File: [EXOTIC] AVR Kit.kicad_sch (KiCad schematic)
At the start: 24 parts, among them J2 AVR-ISP-10, J3 USB_B, J4 Port A, J5 Port B, J6 Port C + D7, J7 Port D, SW1 SW_Push, U1 ATmega32A-P, U6 CH340C, Y1 16 MHz

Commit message: Pre Rev. 4
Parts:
- added F2: Polyfuse_Small, Capacitor_THT:C_Disc_D10.5mm_W5.0mm_P5.00mm, symbol Device:Polyfuse_Small
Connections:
- net +5V: now also F2.1; no longer R1.1, U1.10 (VCC)
- new net +5V_{PPTC}: F2.2, R1.1, U1.10 (VCC)
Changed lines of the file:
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@@
+    (stroke (width 0) (type default))
+  )
+  (wire (pts (xy 110.49 31.75) (xy 110.49 34.29))
     (stroke (width 0) (type default))
   )
@@
     (stroke (width 0) (type default))
   )
+  (wire (pts (xy 110.49 41.91) (xy 110.49 39.37))
+    (stroke (width 0) (type default))
+  )
   (wire (pts (xy 146.05 127) (xy 151.13 127))
     (stroke (width 0) (type default))
@@
     (stroke (width 0) (type default))
   )
-  (wire (pts (xy 90.17 30.48) (xy 92.71 30.48))
-    (stroke (width 0) (type default))
-  )
   (wire (pts (xy 60.96 26.67) (xy 60.96 29.21))
     (stroke (width 0) (type default))
@@
     (stroke (width 0) (type default))
   )
+  (wire (pts (xy 90.17 30.48) (xy 95.25 30.48))
+    (stroke (width 0) (type default))
+  )
   (wire (pts (xy 91.44 121.92) (xy 93.98 121.92))
     (stroke (width 0) (type default))
@@
   )
   (wire (pts (xy 91.44 132.08) (xy 93.98 132.08))
-    (stroke (width 0) (type default))
-  )
-  (wire (pts (xy 92.71 27.94) (xy 92.71 30.48))
     (stroke (width 0) (type default))
   )
@@
   (label "PD5" (at 93.98 132.08 0) (fields_autoplaced)
     (effects (font (size 1.27 1.27)) (justify left bottom))
+  )
+  (global_label "+5V_{PPTC}" (shape input) (at 60.96 26.67 90) (fields_autoplaced)
+    (effects (font (size 1.27 1.27)) (justify left))
+    (property "Intersheetrefs" "${INTERSHEET_REFS}" (at 60.96 15.9414 90)
+      (effects (font (size 1.27 1.27)) (justify left) hide)
+    )
   )
   (global_label "+5V_{NetTie}" (shape input) (at 171.45 34.29 90) (fields_autoplaced)
@@
     )
   )
-  (global_label "+5V_{NetTie}" (shape input) (at 92.71 27.94 90) (fields_autoplaced)
+  (global_label "+5V_{PPTC}" (shape input) (at 97.79 19.05 0) (fields_autoplaced)
     (effects (font (size 1.27 1.27)) (justify left))
-    (property "Intersheetrefs" "${INTERSHEET_REFS}" (at 92.71 16.3888 90)
+    (property "Intersheetrefs" "${INTERSHEET_REFS}" (at 108.5186 19.05 0)
       (effects (font (size 1.27 1.27)) (justify left) hide)
     )
   )
-  (symbol (lib_id "power:+5V") (at 76.2 40.64 0) (unit 1)
-    (in_bom yes) (on_board yes) (dnp no) (fields_autoplaced)
-    (property "Reference" "#PWR06" (at 76.2 44.45 0)
-      (effects (font (size 1.27 1.27)) hide)
-    )
-    (property "Value" "+5V" (at 76.2 36.83 0)
-      (effects (font (size 1.27 1.27)))
-    )
-    (property "Footprint" "" (at 76.2 40.64 0)
-      (effects (font (size 1.27 1.27)) hide)
-    )
-    (property "Datasheet" "" (at 76.2 40.64 0)
+  (global_label "+5V_{PPTC}" (shape output) (at 110.49 41.91 270) (fields_autoplaced)
+    (effects (font (size 1.27 1.27)) (justify right))
+    (property "Intersheetrefs" "${INTERSHEET_REFS}" (at 110.49 52.6386 90)
+      (effects (font (size 1.27 1.27)) (justify right) hide)
+    )
+  )
+  (global_label "+5V_{PPTC}" (shape input) (at 76.2 40.64 90) (fields_autoplaced)
+    (effects (font (size 1.27 1.27)) (justify left))
+    (property "Intersheetrefs" "${INTERSHEET_REFS}" (at 76.2 29.9114 90)
+      (effects (font (size 1.27 1.27)) (justify left) hide)
+    )
+  )
+  (global_label "+5V_{NetTie}" (shape input) (at 95.25 30.48 0) (fields_autoplaced)
+    (effects (font (size 1.27 1.27)) (justify left))
+    (property "Intersheetrefs" "${INTERSHEET_REFS}" (at 106.8012 30.48 0)
+      (effects (font (size 1.27 1.27)) (justify left) hide)
+    )
+  )
+  (symbol (lib_id "power:+5V") (at 110.49 31.75 0) (unit 1)
+    (in_bom yes) (on_board yes) (dnp no)
+    (property "Reference" "#PWR06" (at 110.49 35.56 0)
+      (effects (font (size 1.27 1.27)) hide)
+    )
+    (property "Value" "+5V" (at 110.49 27.94 0)
+      (effects (font (size 1.27 1.27)))
+    )
+    (property "Footprint" "" (at 110.49 31.75 0)
+      (effects (font (size 1.27 1.27)) hide)
+    )
+    (property "Datasheet" "" (at 110.49 31.75 0)
       (effects (font (size 1.27 1.27)) hide)
     )
@@
     )
   )
-  (symbol (lib_id "power:+5V") (at 60.96 26.67 0) (unit 1)
-    (in_bom yes) (on_board yes) (dnp no) (fields_autoplaced)
-    (property "Reference" "#PWR05" (at 60.96 30.48 0)
-      (effects (font (size 1.27 1.27)) hide)
-    )
-    (property "Value" "+5V" (at 60.96 22.86 0)
-      (effects (font (size 1.27 1.27)))
-    )
-    (property "Footprint" "" (at 60.96 26.67 0)
-      (effects (font (size 1.27 1.27)) hide)
-    )
-    (property "Datasheet" "" (at 60.96 26.67 0)
-      (effects (font (size 1.27 1.27)) hide)
-    )
-    (pin "1")
-    (instances
-      (project "[EXOTIC] AVR Kit"
-        (path "/bd689b4b-40d7-46ba-91b6-965ce30f8212"
-          (reference "#PWR05") (unit 1)
-        )
-      )
-      (project "ATMEGA32A Development Board"
-        (path "/e232854a-3fe0-4443-9abe-081b69d86c79"
-          (reference "#PWR08") (unit 1)
-        )
-      )
-    )
-  )
   (symbol (lib_id "Connector:Conn_01x08_Socket") (at 181.61 119.38 0) (unit 1)
     (in_bom yes) (on_board yes) (dnp no) (fields_autoplaced)
@@
         )
       )
+    )
+  )
+  (symbol (lib_id "Device:Polyfuse_Small") (at 110.49 36.83 0) (unit 1)
+    (in_bom yes) (on_board yes) (dnp no) (fields_autoplaced)
+    (property "Reference" "F2" (at 113.03 35.56 0)
+      (effects (font (size 1.27 1.27)) (justify left))
+    )
+    (property "Value" "Polyfuse_Small" (at 113.03 38.1 0)
+      (effects (font (size 1.27 1.27)) (justify left))
+    )
+    (property "Footprint" "Capacitor_THT:C_Disc_D10.5mm_W5.0mm_P5.00mm" (at 111.76 41.91 0)
+      (effects (font (size 1.27 1.27)) (justify left) hide)
+    )
+    (property "Datasheet" "~" (at 110.49 36.83 0)
+      (effects (font (size 1.27 1.27)) hide)
+    )
+    (pin "1")
+    (pin "2")
+    (instances
+      (project "[EXOTIC] AVR Kit"
+        (path "/bd689b4b-40d7-46ba-91b6-965ce30f8212"
+          (reference "F2") (unit 1)
+        )
+      )

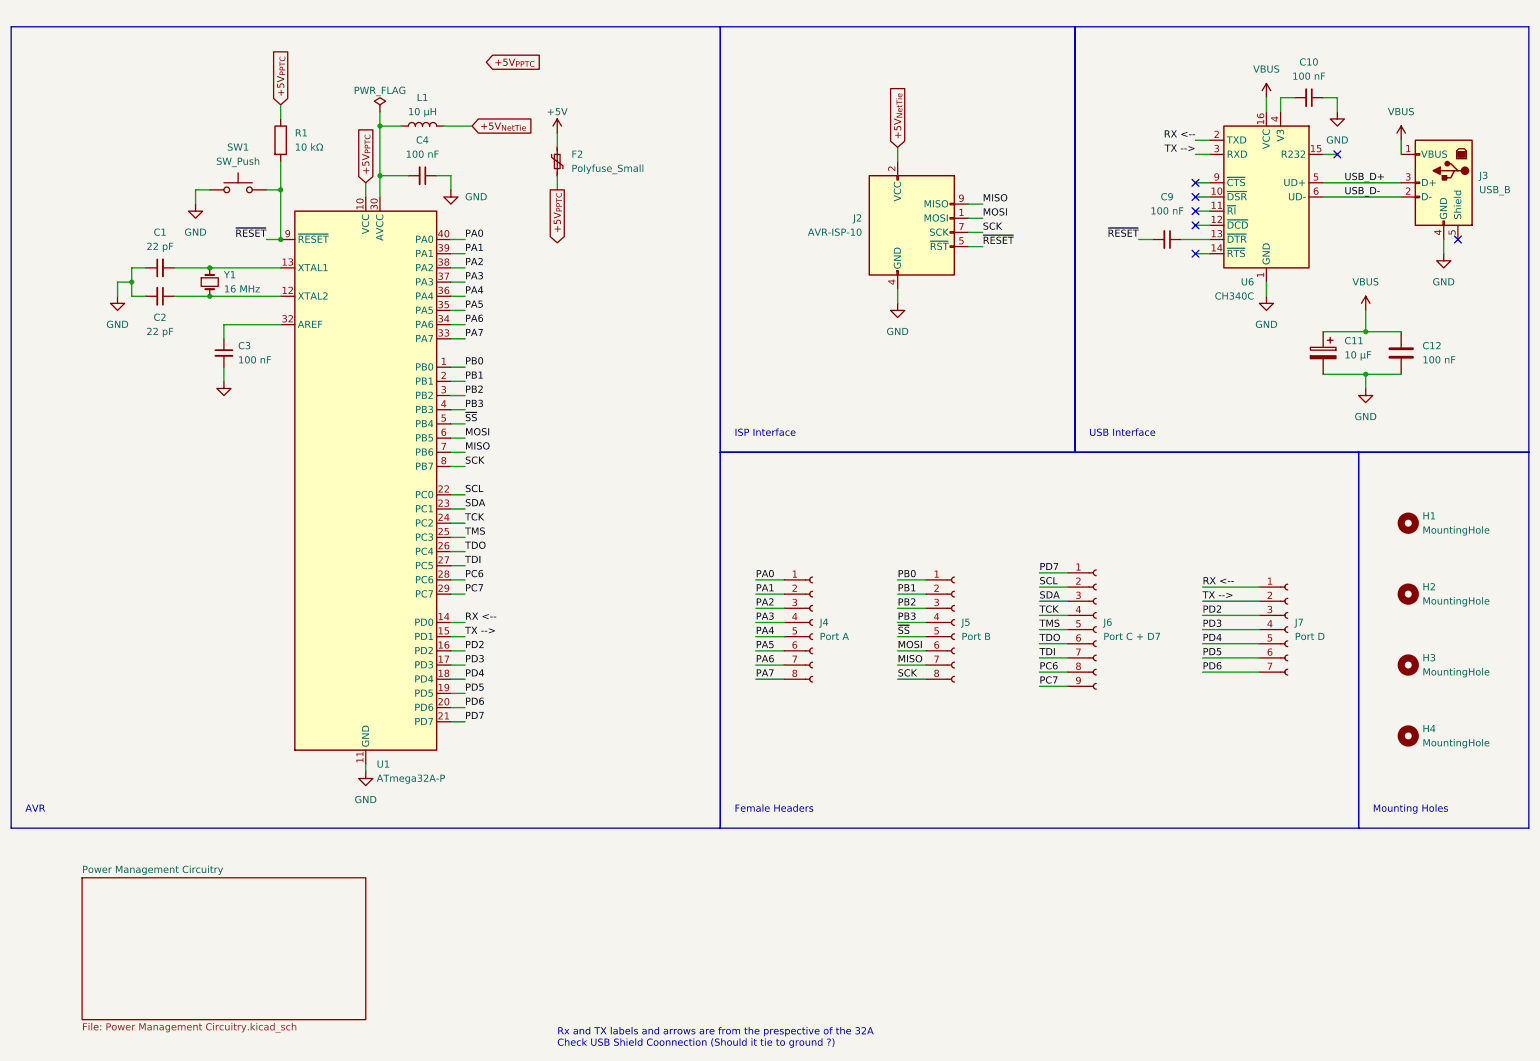
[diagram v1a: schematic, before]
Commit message: Migrated from KiCAD 7.0 to 8.0
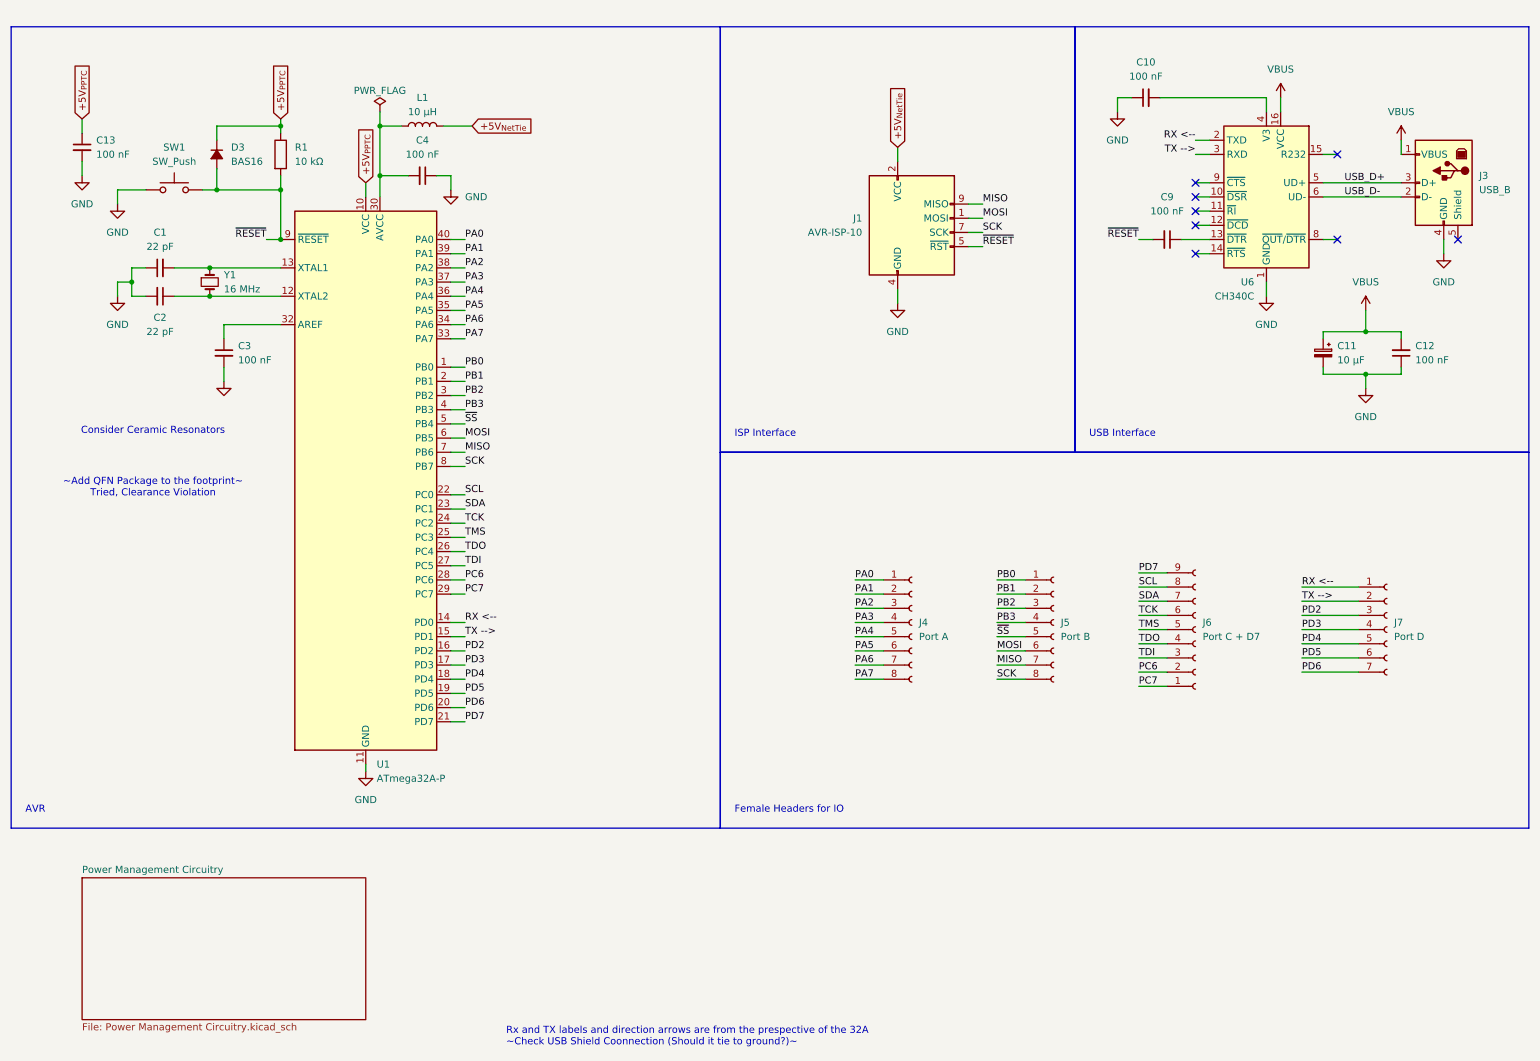
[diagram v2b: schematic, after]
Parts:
- removed F2: Polyfuse_Small, Capacitor_THT:C_Disc_D10.5mm_W5.0mm_P5.00mm, symbol Device:Polyfuse_Small
- removed H1, H2, H3, H4: MountingHole, MountingHole:MountingHole_2.2mm_M2_Pad, symbol Mechanical:MountingHole
- added C13: 100 nF, Capacitor_SMD:C_1206_3216Metric_Pad1.33x1.80mm_HandSolder, symbol Device:C_Small
- added D3: BAS16, Package_TO_SOT_SMD:SOT-23_Handsoldering, symbol Device:D_Small_Filled
- C11: symbol Device:C_Polarized -> Device:C_Polarized_Small
- C12: symbol Device:C -> Device:C_Small
- renumbered J2 to J1
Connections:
- net +5V_{PPTC}: now also C13.1, D3.1 (K)
- net GND: now also C13.2
- net PC6: now also J6.2 (Pin_2); no longer J6.8 (Pin_8)
- net PC7: now also J6.1 (Pin_1); no longer J6.9 (Pin_9)
- net PD7: now also J6.9 (Pin_9); no longer J6.1 (Pin_1)
- net SCL: now also J6.8 (Pin_8); no longer J6.2 (Pin_2)
- net SDA: now also J6.7 (Pin_7); no longer J6.3 (Pin_3)
- net TCK: now also J6.6 (Pin_6); no longer J6.4 (Pin_4)
- net TDI: now also J6.3 (Pin_3); no longer J6.7 (Pin_7)
- net TDO: now also J6.4 (Pin_4); no longer J6.6 (Pin_6)
- net ~{RESET}: now also D3.2 (A)
- no-connect marks 7 -> 8
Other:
- note added: "Consider Ceramic Resonators"
- note added: "Female Headers for IO"
- note added: "Rx and TX labels and direction arrows are from the prespective of the 32A ~Check USB Shield Coonnection (Should it tie to ground?)~"
- note added: "~Add QFN Package to the footprint~ Tried, Clearance Violation"
- note removed: "Female Headers"
- note removed: "Mounting Holes"
- note removed: "Rx and TX labels and arrows are from the prespective of the 32A Check USB Shield Coonnection (Should it tie to ground ?)"
- company: Team Exotic -> Exotic Racing Team
- moved on the sheet: C10, C12, J4, J5, J6, J7, R1, SW1
